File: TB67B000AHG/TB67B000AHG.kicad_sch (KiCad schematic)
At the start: 0 parts

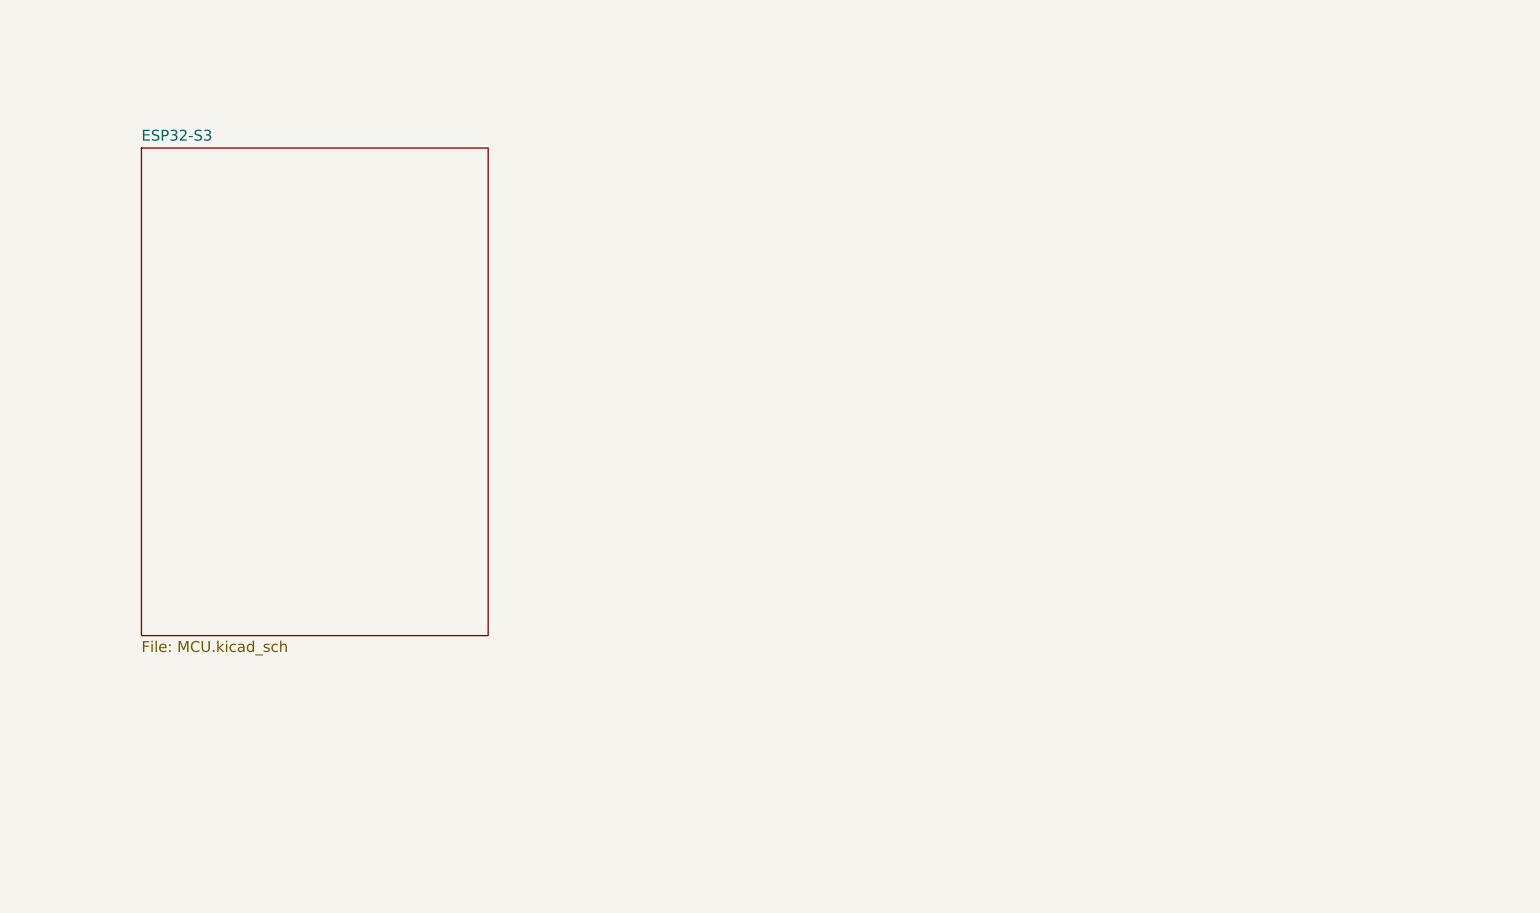
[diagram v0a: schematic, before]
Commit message: Add TB67B000AHG template circuit
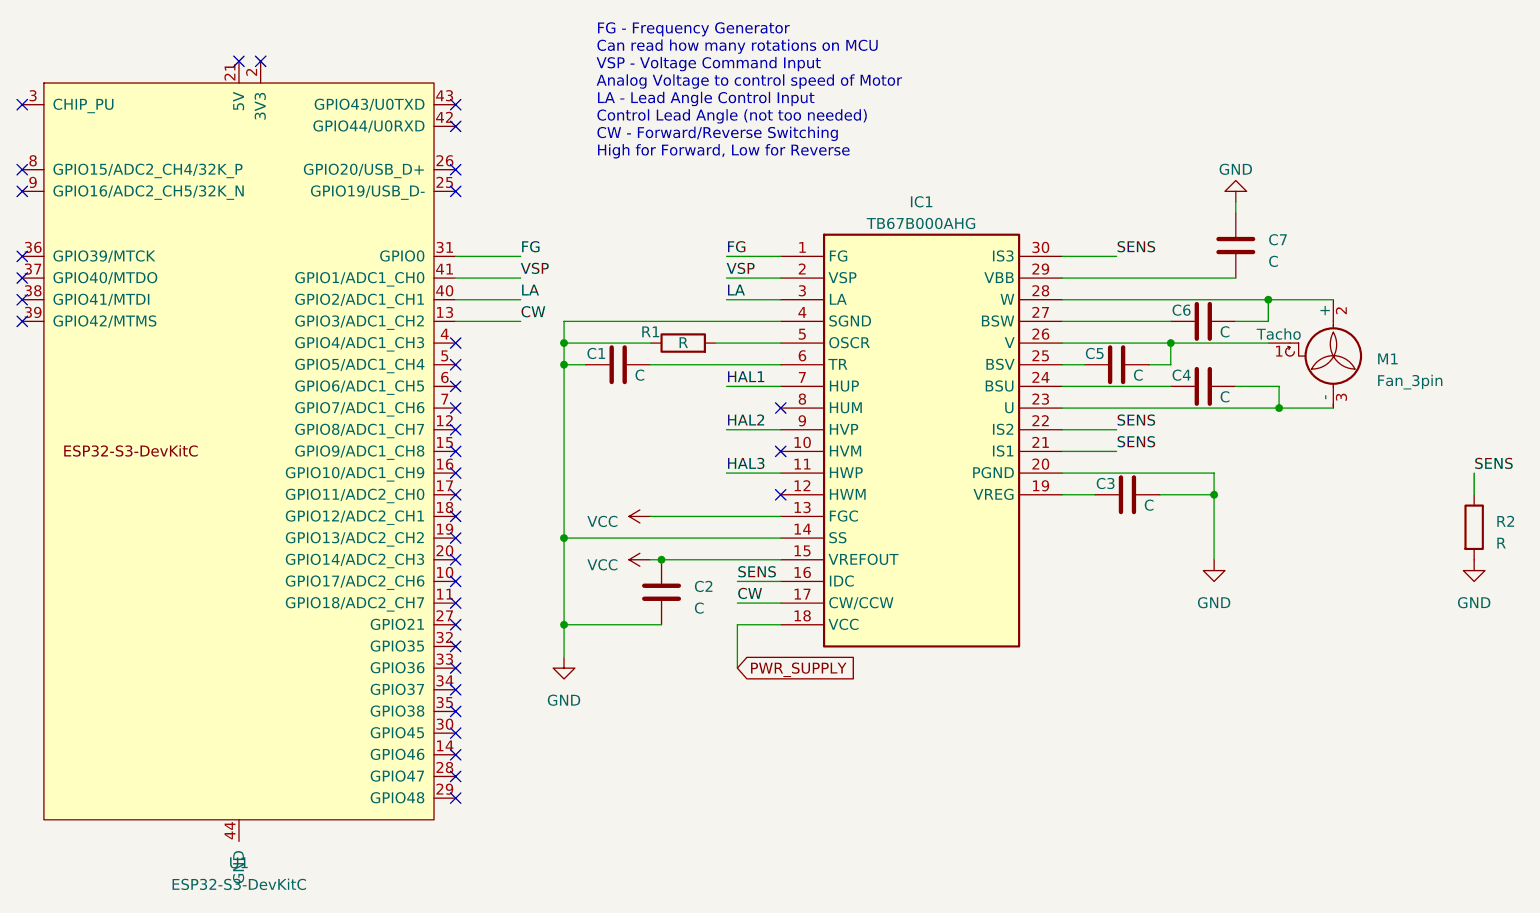
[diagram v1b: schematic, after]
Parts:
- added C1, C2, C3, C4, C5, C6, C7: C, symbol Device:C
- added IC1: TB67B000AHG, TB67B000AHG, symbol TB67B000AHG:TB67B000AHG
- added M1: Fan_3pin, symbol Motor:Fan_3pin
- added R1, R2: R, symbol Device:R
- added U1: ESP32-S3-DevKitC, Espressif:ESP32-S3-DevKitC, symbol Espressif:ESP32-S3-DevKitC
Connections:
- new net: C3.1, IC1.19 (VREG)
- new net: C4.2, IC1.23 (U), M1.3 (-)
- new net: C4.1, IC1.24 (BSU)
- new net: C5.1, IC1.25 (BSV)
- new net: C5.2, IC1.26 (V), M1.1 (Tacho)
- new net: C6.1, IC1.27 (BSW)
- new net: C6.2, IC1.28 (W), M1.2 (+)
- new net: C7.2, IC1.29 (VBB)
- new net: IC1.5 (OSCR), R1.2
- new net: C1.2, IC1.6 (TR)
- new net: U1.1 (3V3), U1.2 (3V3)
- new net: U1.22 (GND), U1.23 (GND), U1.24 (GND), U1.44 (GND)
- new net CW: IC1.17 (CW/CCW), U1.13 (GPIO3/ADC1_CH2)
- new net FG: IC1.1 (FG), U1.31 (GPIO0)
- new net GND: C1.1, C2.2, C3.2, C7.1, IC1.14 (SS), IC1.20 (PGND), IC1.4 (SGND), R1.1, R2.2
- new net HAL1: IC1.7 (HUP)
- new net HAL2: IC1.9 (HVP)
- new net HAL3: IC1.11 (HWP)
- new net LA: IC1.3 (LA), U1.40 (GPIO2/ADC1_CH1)
- new net PWR_SUPPLY: IC1.18 (VCC)
- new net SENS: IC1.16 (IDC), IC1.21 (IS1), IC1.22 (IS2), IC1.30 (IS3), R2.1
- new net VCC: C2.1, IC1.13 (FGC), IC1.15 (VREFOUT)
- new net VSP: IC1.2 (VSP), U1.41 (GPIO1/ADC1_CH0)
- no-connect marks 0 -> 38
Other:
- removed sheet ESP32-S3
- note added: "FG - Frequency Generator Can read how many rotations on MCU VSP - Voltage Command Input Analog Voltage to control speed of Motor LA - Lead Angle Control Input Control Lead Angle (not too needed) CW - Forward/Reverse Switching High for Forward, Low for Reverse"
